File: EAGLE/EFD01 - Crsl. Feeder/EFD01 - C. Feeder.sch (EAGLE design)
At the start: 40 parts, among them J1 MOD TOOL, J2 SPI, J3 MOT, J4 FTDI, Q1 BSS138, Q2 16MHz, U1 SP3485, U2 TCST1030, U3 ATMEGA238, U4 DRV8825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

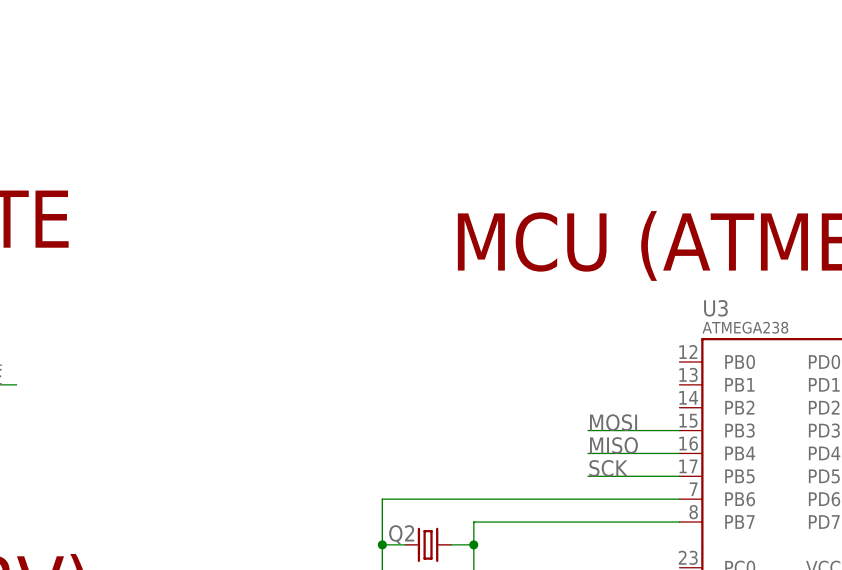
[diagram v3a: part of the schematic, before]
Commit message: Made REV 2 modifications, including increasing width of power traces, adding vias to power traces, and addition of LEDs to all modular tools. Catch diodes added to ESOL01 board to prevent coils from creating problems "upstream"
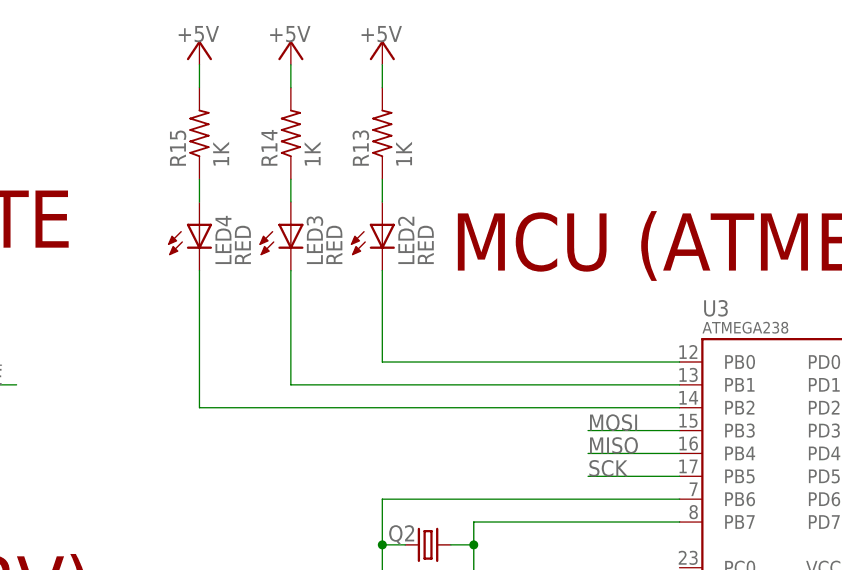
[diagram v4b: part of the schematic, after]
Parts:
- added LED2, LED3, LED4: RED, TinWhiskers:CPL-LED-0603-RED
- added R13, R14, R15: 1K, TinWhiskers:CPL-RES-0603-1K-0.1W
- C10, C11, C12, C13: PARTNO (none) -> UMK107B7104KA-T
- C9: PARTNO (none) -> EMVA500ADA101MHA0G
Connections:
- new net N$10: LED2.A, R13.1
- new net N$11: LED3.C, U3.PB1
- new net N$12: LED3.A, R14.1
- new net N$17: LED4.C, U3.PB2
- new net N$18: LED4.A, R15.1
- new net N$7: LED2.C, U3.PB0
- net +5V: now also R13.2, R14.2, R15.2
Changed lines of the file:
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@@
 <attribute name="PARTNO" value="*"/>
 </part>
-<part name="C9" library="TinWhiskers" deviceset="CPL-CAP-ALU-SMD-100UF-50V" device="" value="100uF"/>
+<part name="C9" library="TinWhiskers" deviceset="CPL-CAP-ALU-SMD-100UF-50V" device="" value="100uF">
+<attribute name="PARTNO" value="EMVA500ADA101MHA0G"/>
+</part>
 <part name="SUPPLY11" library="TinWhiskers" deviceset="GND" device=""/>
 <part name="P+13" library="supply1" deviceset="+24V" device=""/>
-<part name="C10" library="TinWhiskers" deviceset="CPL-CAP-X7R-0603-0.1UF-35V" device="" value="0.1uF"/>
+<part name="C10" library="TinWhiskers" deviceset="CPL-CAP-X7R-0603-0.1UF-35V" device="" value="0.1uF">
+<attribute name="PARTNO" value="UMK107B7104KA-T"/>
+</part>
 <part name="SUPPLY19" library="TinWhiskers" deviceset="GND" device=""/>
-<part name="C11" library="TinWhiskers" deviceset="CPL-CAP-X7R-0603-0.1UF-35V" device="" value="0.1uF"/>
+<part name="C11" library="TinWhiskers" deviceset="CPL-CAP-X7R-0603-0.1UF-35V" device="" value="0.1uF">
+<attribute name="PARTNO" value="UMK107B7104KA-T"/>
+</part>
 <part name="P+14" library="supply1" deviceset="+5V" device=""/>
 <part name="SUPPLY20" library="TinWhiskers" deviceset="GND" device=""/>
-<part name="C12" library="TinWhiskers" deviceset="CPL-CAP-X7R-0603-0.1UF-35V" device="" value="0.1uF"/>
+<part name="C12" library="TinWhiskers" deviceset="CPL-CAP-X7R-0603-0.1UF-35V" device="" value="0.1uF">
+<attribute name="PARTNO" value="UMK107B7104KA-T"/>
+</part>
 <part name="P+15" library="supply1" deviceset="+5V" device=""/>
 <part name="SUPPLY21" library="TinWhiskers" deviceset="GND" device=""/>
-<part name="C13" library="TinWhiskers" deviceset="CPL-CAP-X7R-0603-0.1UF-35V" device="" value="0.1uF"/>
+<part name="C13" library="TinWhiskers" deviceset="CPL-CAP-X7R-0603-0.1UF-35V" device="" value="0.1uF">
+<attribute name="PARTNO" value="UMK107B7104KA-T"/>
+</part>
 <part name="P+16" library="supply1" deviceset="+5V" device=""/>
 <part name="SUPPLY24" library="TinWhiskers" deviceset="GND" device=""/>
+<part name="LED2" library="TinWhiskers" deviceset="CPL-LED-0603-RED" device="" value="RED">
+<attribute name="PARTNO" value="SML-D12M8WT86"/>
+</part>
+<part name="P+17" library="supply1" deviceset="+5V" device=""/>
+<part name="R13" library="TinWhiskers" deviceset="CPL-RES-0603-1K-0.1W" device="" value="1K">
+<attribute name="PARTNO" value="RC0603FR-071KL"/>
+</part>
+<part name="LED3" library="TinWhiskers" deviceset="CPL-LED-0603-RED" device="" value="RED">
+<attribute name="PARTNO" value="SML-D12M8WT86"/>
+</part>
+<part name="P+18" library="supply1" deviceset="+5V" device=""/>
+<part name="R14" library="TinWhiskers" deviceset="CPL-RES-0603-1K-0.1W" device="" value="1K">
+<attribute name="PARTNO" value="RC0603FR-071KL"/>
+</part>
+<part name="LED4" library="TinWhiskers" deviceset="CPL-LED-0603-RED" device="" value="RED">
+<attribute name="PARTNO" value="SML-D12M8WT86"/>
+</part>
+<part name="P+19" library="supply1" deviceset="+5V" device=""/>
+<part name="R15" library="TinWhiskers" deviceset="CPL-RES-0603-1K-0.1W" device="" value="1K">
+<attribute name="PARTNO" value="RC0603FR-071KL"/>
+</part>
 </parts>
 <sheets>
@@
 <attribute name="NAME" x="273.939" y="96.774" size="1.778" layer="95" rot="R90"/>
 <attribute name="VALUE" x="276.479" y="92.456" size="1.778" layer="96" rot="R90"/>
+<attribute name="PARTNO" x="274.32" y="101.6" size="1.778" layer="96" display="off"/>
 </instance>
 <instance part="SUPPLY11" gate="GND" x="274.32" y="91.44"/>
@@
 <attribute name="NAME" x="360.299" y="183.642" size="1.778" layer="95" rot="R90"/>
 <attribute name="VALUE" x="362.839" y="181.102" size="1.778" layer="96" rot="R90"/>
+<attribute name="PARTNO" x="360.68" y="190.5" size="1.778" layer="96" display="off"/>
 </instance>
 <instance part="SUPPLY19" gate="GND" x="360.68" y="180.34"/>
@@
 <attribute name="NAME" x="187.579" y="59.182" size="1.778" layer="95" rot="R90"/>
 <attribute name="VALUE" x="190.119" y="56.642" size="1.778" layer="96" rot="R90"/>
+<attribute name="PARTNO" x="187.96" y="66.04" size="1.778" layer="96" display="off"/>
 </instance>
 <instance part="P+14" gate="1" x="187.96" y="73.66" smashed="yes">
@@
 <attribute name="NAME" x="63.119" y="76.962" size="1.778" layer="95" rot="R90"/>
 <attribute name="VALUE" x="65.659" y="74.422" size="1.778" layer="96" rot="R90"/>
+<attribute name="PARTNO" x="63.5" y="83.82" size="1.778" layer="96" display="off"/>
 </instance>
 <instance part="P+15" gate="1" x="63.5" y="91.44" smashed="yes">
@@
 <attribute name="NAME" x="179.959" y="193.802" size="1.778" layer="95" rot="R90"/>
 <attribute name="VALUE" x="182.499" y="191.262" size="1.778" layer="96" rot="R90"/>
+<attribute name="PARTNO" x="180.34" y="200.66" size="1.778" layer="96" display="off"/>
 </instance>
 <instance part="P+16" gate="1" x="180.34" y="208.28" smashed="yes">
@@
 </instance>
 <instance part="SUPPLY24" gate="GND" x="180.34" y="190.5"/>
+<instance part="LED2" gate="G$1" x="279.4" y="213.36" smashed="yes">
+<attribute name="NAME" x="282.956" y="208.788" size="1.778" layer="95" rot="R90"/>
+<attribute name="VALUE" x="285.115" y="208.788" size="1.778" layer="96" rot="R90"/>
+<attribute name="PARTNO" x="279.4" y="213.36" size="2.54" layer="96" ratio="10" display="off"/>
+</instance>
+<instance part="P+17" gate="1" x="279.4" y="233.68" smashed="yes">
+<attribute name="VALUE" x="276.86" y="233.68" size="1.778" layer="96"/>
+</instance>
+<instance part="R13" gate="G$1" x="279.4" y="223.52" rot="R90">
+<attribute name="PARTNO" x="279.4" y="223.52" size="2.54" layer="96" ratio="10" display="off"/>
+</instance>
+<instance part="LED3" gate="G$1" x="269.24" y="213.36" smashed="yes">
+<attribute name="NAME" x="272.796" y="208.788" size="1.778" layer="95" rot="R90"/>
+<attribute name="VALUE" x="274.955" y="208.788" size="1.778" layer="96" rot="R90"/>
+<attribute name="PARTNO" x="269.24" y="213.36" size="2.54" layer="96" ratio="10" display="off"/>
+</instance>
+<instance part="P+18" gate="1" x="269.24" y="233.68" smashed="yes">
+<attribute name="VALUE" x="266.7" y="233.68" size="1.778" layer="96"/>
+</instance>
+<instance part="R14" gate="G$1" x="269.24" y="223.52" rot="R90">
+<attribute name="PARTNO" x="269.24" y="223.52" size="2.54" layer="96" ratio="10" display="off"/>
+</instance>
+<instance part="LED4" gate="G$1" x="259.08" y="213.36" smashed="yes">
+<attribute name="NAME" x="262.636" y="208.788" size="1.778" layer="95" rot="R90"/>
+<attribute name="VALUE" x="264.795" y="208.788" size="1.778" layer="96" rot="R90"/>
+<attribute name="PARTNO" x="259.08" y="213.36" size="2.54" layer="96" ratio="10" display="off"/>
+</instance>
+<instance part="P+19" gate="1" x="259.08" y="233.68" smashed="yes">
+<attribute name="VALUE" x="256.54" y="233.68" size="1.778" layer="96"/>
+</instance>
+<instance part="R15" gate="G$1" x="259.08" y="223.52" rot="R90">
+<attribute name="PARTNO" x="259.08" y="223.52" size="2.54" layer="96" ratio="10" display="off"/>
+</instance>
 </instances>
 <busses>
@@
 <pinref part="C13" gate="G$1" pin="2"/>
 <wire x1="180.34" y1="205.74" x2="180.34" y2="203.2" width="0.1524" layer="91"/>
+</segment>
+<segment>
+<pinref part="P+17" gate="1" pin="+5V"/>
+<pinref part="R13" gate="G$1" pin="2"/>
+<wire x1="279.4" y1="231.14" x2="279.4" y2="228.6" width="0.1524" layer="91"/>
+</segment>
+<segment>
+<pinref part="P+18" gate="1" pin="+5V"/>
+<pinref part="R14" gate="G$1" pin="2"/>
+<wire x1="269.24" y1="231.14" x2="269.24" y2="228.6" width="0.1524" layer="91"/>
+</segment>
+<segment>
+<pinref part="P+19" gate="1" pin="+5V"/>
+<pinref part="R15" gate="G$1" pin="2"/>
+<wire x1="259.08" y1="231.14" x2="259.08" y2="228.6" width="0.1524" layer="91"/>
 </segment>
 </net>
@@
 </segment>
 </net>
+<net name="N$7" class="0">
+<segment>
+<pinref part="LED2" gate="G$1" pin="C"/>
+<pinref part="U3" gate="G$1" pin="PB0"/>
+<wire x1="312.42" y1="198.12" x2="279.4" y2="198.12" width="0.1524" layer="91"/>
+<wire x1="279.4" y1="198.12" x2="279.4" y2="208.28" width="0.1524" layer="91"/>
+</segment>
+</net>
+<net name="N$10" class="0">
+<segment>
+<pinref part="R13" gate="G$1" pin="1"/>
+<pinref part="LED2" gate="G$1" pin="A"/>
+<wire x1="279.4" y1="218.44" x2="279.4" y2="215.9" width="0.1524" layer="91"/>
+</segment>
+</net>
+<net name="N$11" class="0">
+<segment>
+<pinref part="LED3" gate="G$1" pin="C"/>
+<pinref part="U3" gate="G$1" pin="PB1"/>
+<wire x1="312.42" y1="195.58" x2="269.24" y2="195.58" width="0.1524" layer="91"/>
+<wire x1="269.24" y1="195.58" x2="269.24" y2="208.28" width="0.1524" layer="91"/>
+</segment>
+</net>
+<net name="N$12" class="0">
+<segment>
+<pinref part="R14" gate="G$1" pin="1"/>
+<pinref part="LED3" gate="G$1" pin="A"/>
+<wire x1="269.24" y1="218.44" x2="269.24" y2="215.9" width="0.1524" layer="91"/>
+</segment>
+</net>
+<net name="N$17" class="0">
+<segment>
+<pinref part="LED4" gate="G$1" pin="C"/>
+<pinref part="U3" gate="G$1" pin="PB2"/>
+<wire x1="312.42" y1="193.04" x2="259.08" y2="193.04" width="0.1524" layer="91"/>
+<wire x1="259.08" y1="193.04" x2="259.08" y2="208.28" width="0.1524" layer="91"/>
+</segment>
+</net>
+<net name="N$18" class="0">
+<segment>
+<pinref part="R15" gate="G$1" pin="1"/>
+<pinref part="LED4" gate="G$1" pin="A"/>
+<wire x1="259.08" y1="218.44" x2="259.08" y2="215.9" width="0.1524" layer="91"/>
+</segment>
+</net>
